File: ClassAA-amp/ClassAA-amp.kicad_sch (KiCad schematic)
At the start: 0 parts

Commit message: 回路図大体完成
定数は未決定
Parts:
- added C1, C2, C3, C4, C5, C6, C7, C8: C, symbol Device:C
- added J1, J2: AudioJack3, symbol Connector_Audio:AudioJack3
- added J3: Conn_01x03_Pin, symbol Connector:Conn_01x03_Pin
- added R1, R10, R11, R12, R13, R14, R15, R16, R2, R3, R4, R5, R6, R7, R8, R9: R, symbol Device:R
- added RV1: R_Potentiometer_Dual_Separate, symbol Device:R_Potentiometer_Dual_Separate
- added U1, U2: Opamp_Dual, symbol Device:Opamp_Dual
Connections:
- new net: R1.1, R2.1, U1.3 (+), U1.7
- new net: C1.2, R2.2, R4.1, R5.1, R6.2
- new net: R3.2, R4.2, U1.2 (-)
- new net: R1.2, R3.1, U1.1
- new net: R10.2, R12.1, U2.1
- new net: R12.2, R13.2, U2.2 (-)
- new net: C2.1, R8.1, R9.1, U2.6 (-)
- new net: C4.1, RV1.5
- new net: C4.2, R16.1, U2.5 (+)
- new net: C3.2, R15.1, U1.5 (+)
- new net: C1.1, R6.1, R7.1, U1.6 (-)
- new net: C3.1, RV1.2
- new net: C2.2, R11.2, R13.1, R14.1, R9.2
- new net: R10.1, R11.1, U2.3 (+), U2.7
- new net GND: C5.2, C6.1, C7.2, C8.1, J1.S, J2.S, J3.2 (Pin_2), R15.2, R16.2, R7.2, R8.2, RV1.3, RV1.6
- new net L_IN: J1.T, RV1.4
- new net L_OUT: J2.T, R14.2
- new net R_IN: J1.R, RV1.1
- new net R_OUT: J2.R, R5.2
- new net VDD: C5.1, C7.1, J3.1 (Pin_1), U1.8 (V+), U2.8 (V+)
- new net VEE: C6.2, C8.2, J3.3 (Pin_3), U1.4 (V-), U2.4 (V-)

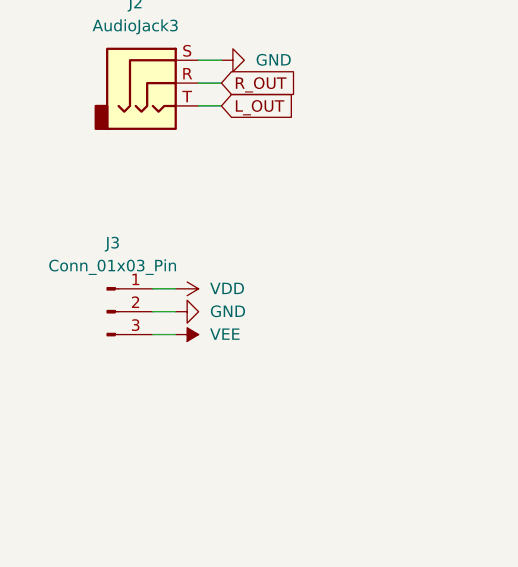
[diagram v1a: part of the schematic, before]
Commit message: コネクタのシンボル変更
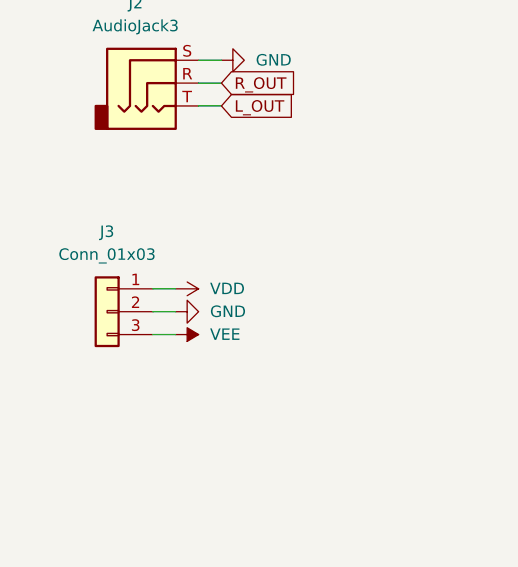
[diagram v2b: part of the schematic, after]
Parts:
- removed J3: Conn_01x03_Pin, symbol Connector:Conn_01x03_Pin
- added J3: Conn_01x03, symbol Connector_Generic:Conn_01x03
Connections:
- net GND: now also J3.2 (Pin_2)
- net VDD: now also J3.1 (Pin_1)
- net VEE: now also J3.3 (Pin_3)

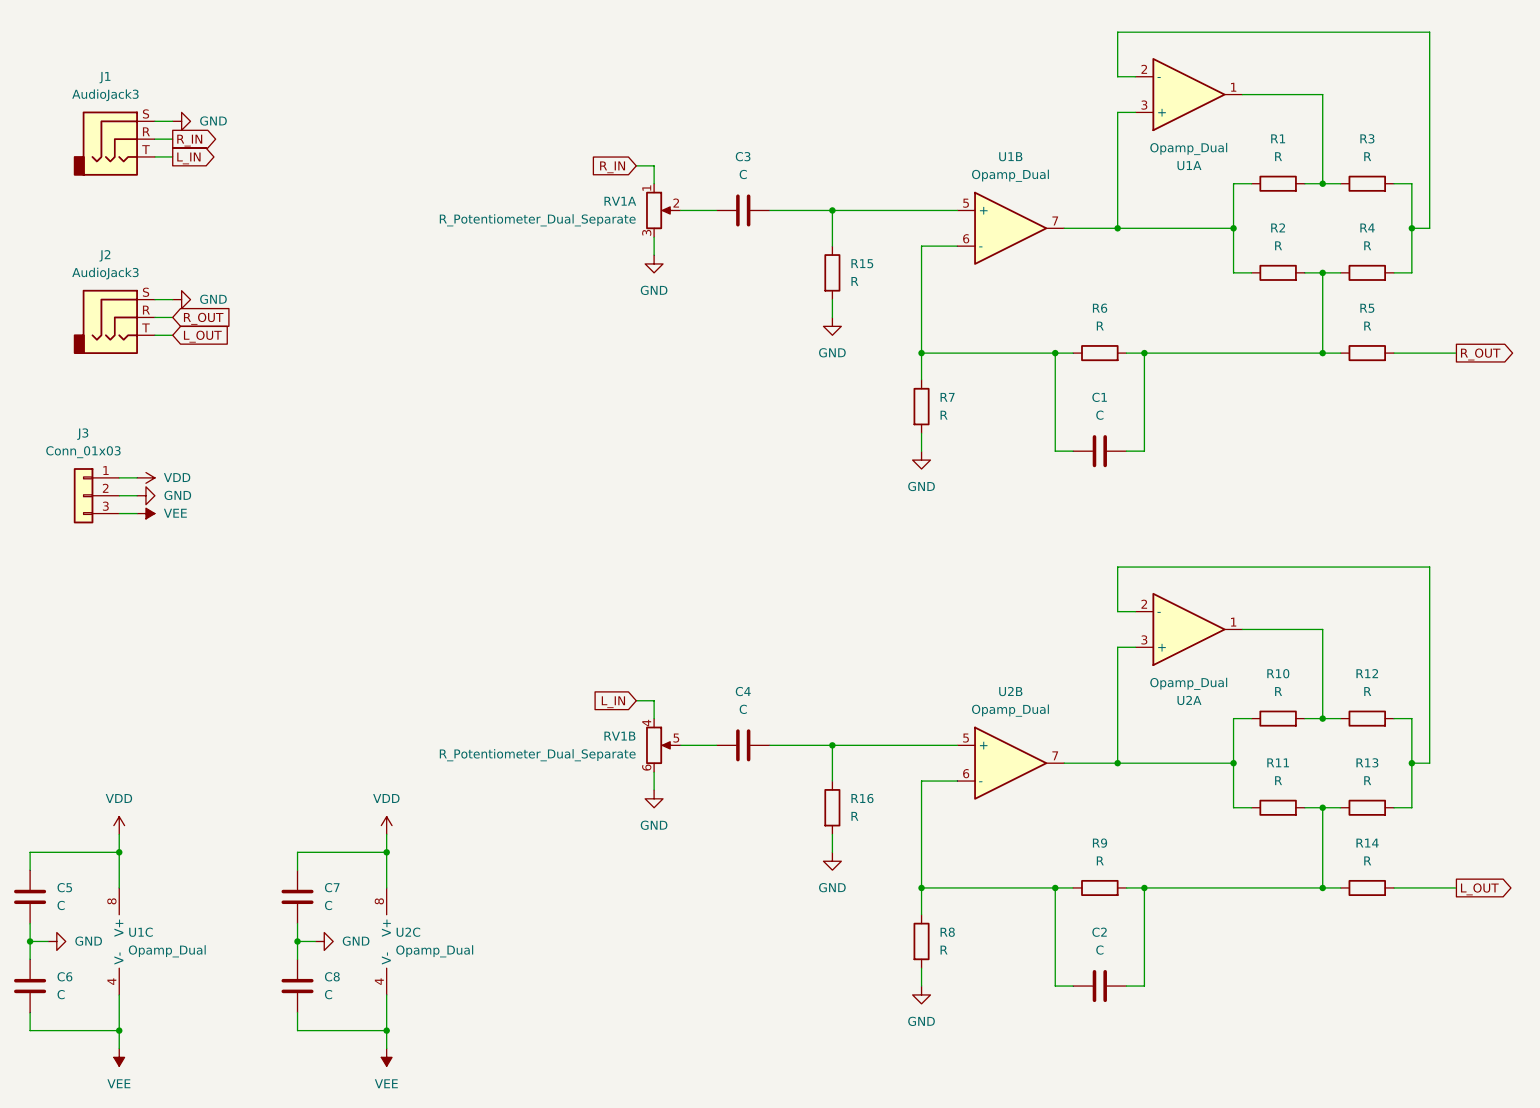
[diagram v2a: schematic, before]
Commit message: 定数決めとアノテーション
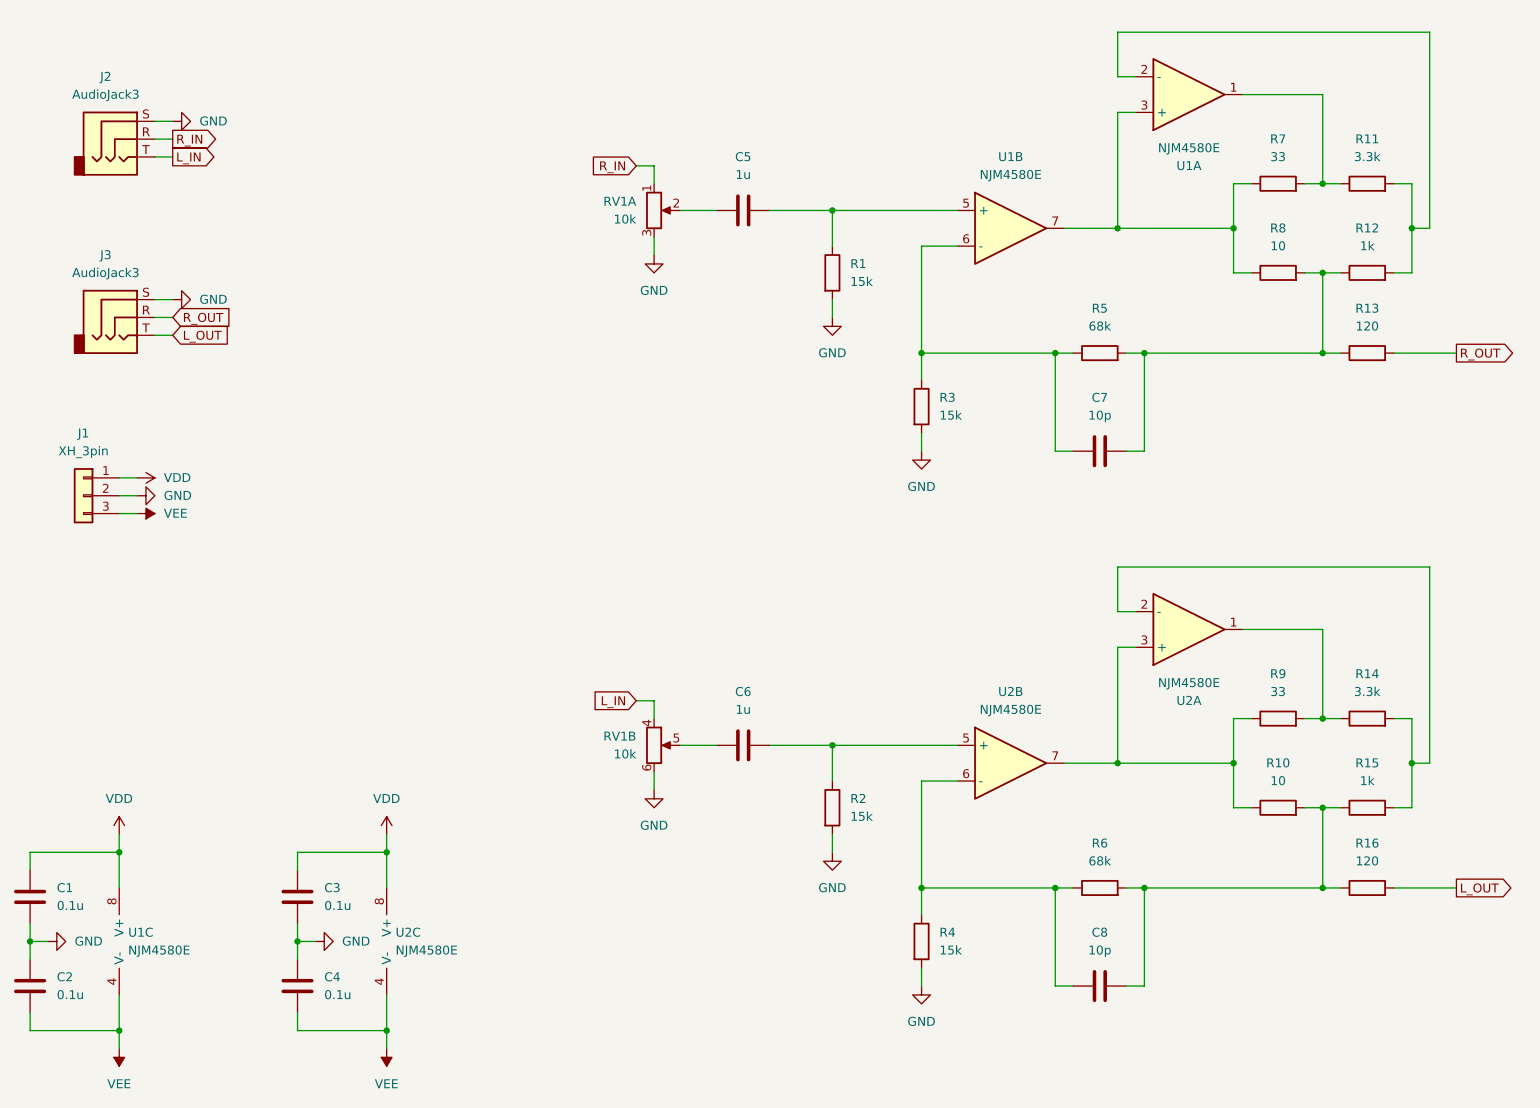
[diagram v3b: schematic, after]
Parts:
- C1: renamed from C5; value C -> 0.1u
- C2: renamed from C6; value C -> 0.1u
- C3: renamed from C7; value C -> 0.1u
- C4: renamed from C8; value C -> 0.1u
- C5: renamed from C3; value C -> 1u
- C6: renamed from C4; value C -> 1u
- C7: renamed from C1; value C -> 10p
- C8: renamed from C2; value C -> 10p
- J1: renamed from J3; value Conn_01x03 -> XH_3pin
- R1: renamed from R15; value R -> 15k
- R10: renamed from R11; value R -> 10
- R11: renamed from R3; value R -> 3.3k
- R12: renamed from R4; value R -> 1k
- R13: renamed from R5; value R -> 120
- R14: renamed from R12; value R -> 3.3k
- R15: renamed from R13; value R -> 1k
- R16: renamed from R14; value R -> 120
- R2: renamed from R16; value R -> 15k
- R3: renamed from R7; value R -> 15k
- R4: renamed from R8; value R -> 15k
- R5: renamed from R6; value R -> 68k
- R6: renamed from R9; value R -> 68k
- R7: renamed from R1; value R -> 33
- R8: renamed from R2; value R -> 10
- R9: renamed from R10; value R -> 33
- RV1: value R_Potentiometer_Dual_Separate -> 10k
- U1, U2: value Opamp_Dual -> NJM4580E
- renumbered J1 to J2, J2 to J3

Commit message: 位相補償の値変更、とりあえずは未実装
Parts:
- C7, C8: value 10p -> 6.8p; now not fitted
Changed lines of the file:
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@@
   )
   (symbol (lib_id "Device:C") (at 190.5 158.75 90) (unit 1)
-    (in_bom yes) (on_board yes) (dnp no) (fields_autoplaced)
+    (in_bom yes) (on_board yes) (dnp yes) (fields_autoplaced)
     (property "Reference" "C8" (at 190.5 151.13 90)
       (effects (font (size 1.27 1.27)))
     )
-    (property "Value" "10p" (at 190.5 153.67 90)
+    (property "Value" "6.8p" (at 190.5 153.67 90)
       (effects (font (size 1.27 1.27)))
     )
@@
   )
   (symbol (lib_id "Device:C") (at 190.5 82.55 90) (unit 1)
-    (in_bom yes) (on_board yes) (dnp no) (fields_autoplaced)
+    (in_bom yes) (on_board yes) (dnp yes) (fields_autoplaced)
     (property "Reference" "C7" (at 190.5 74.93 90)
       (effects (font (size 1.27 1.27)))
     )
-    (property "Value" "10p" (at 190.5 77.47 90)
-      (effects (font (size 1.27 1.27)))
-    )
+    (property "Value" "6.8p" (at 190.5 77.47 90)
+      (effects (font (size 1.27 1.27)))
+    )

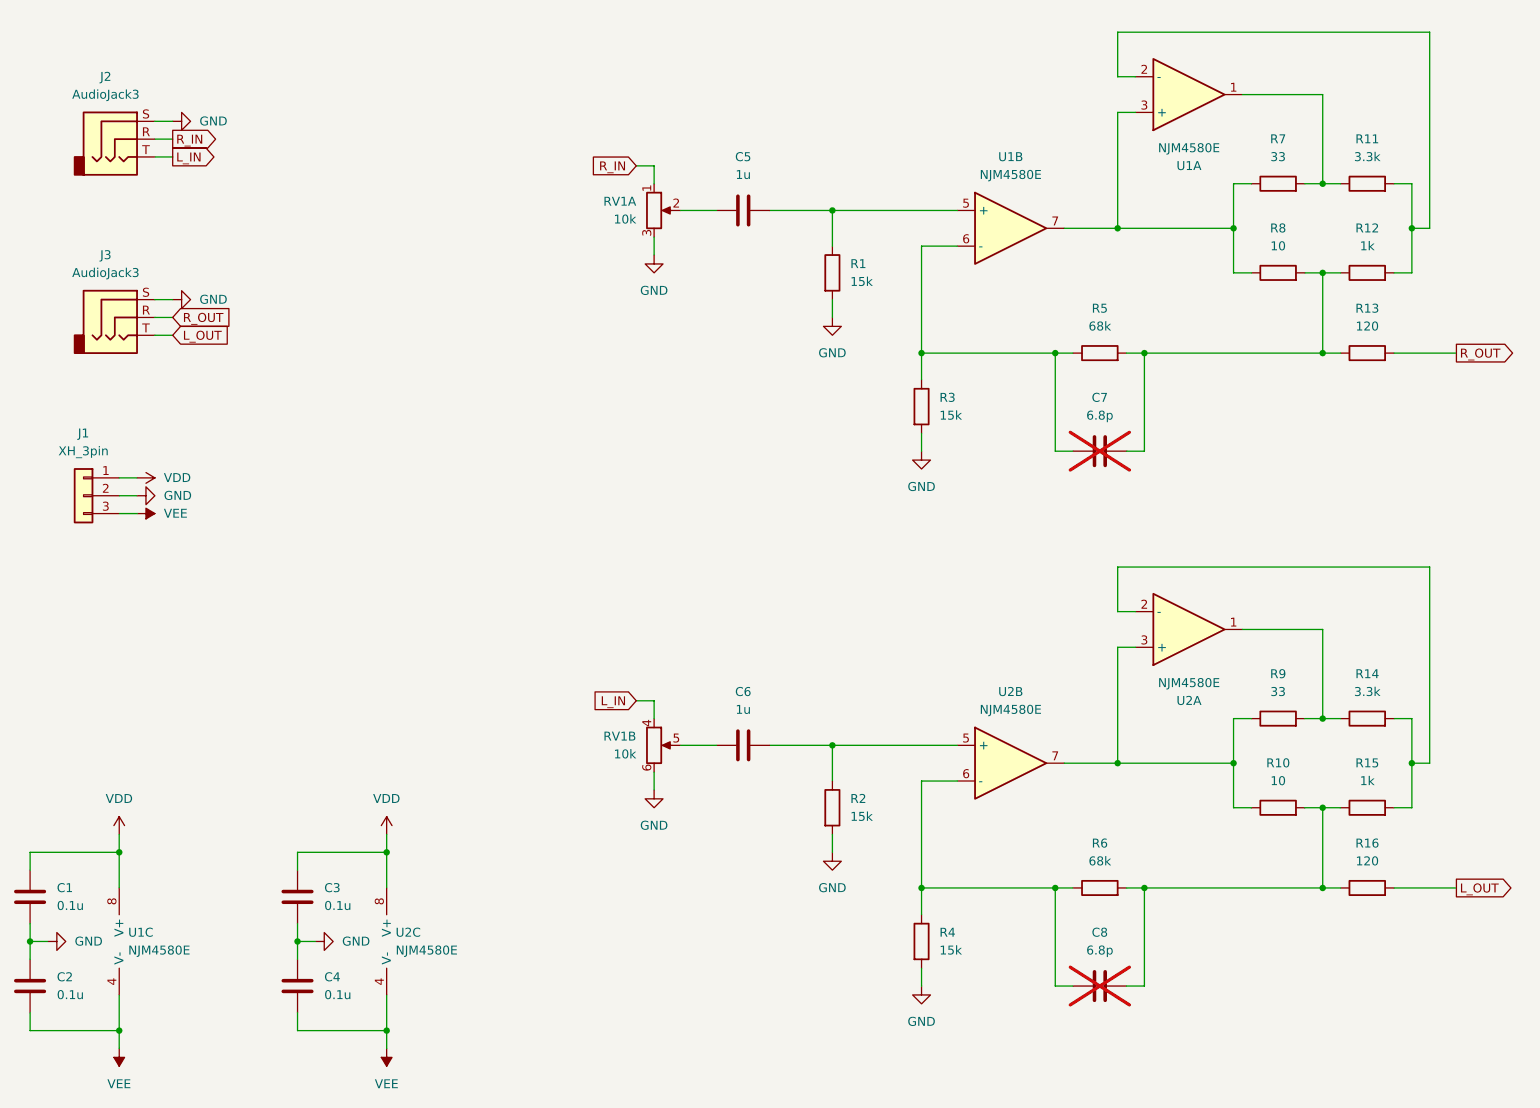
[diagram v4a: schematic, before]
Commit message: C-ampをNJM4580からNJM4556に変更
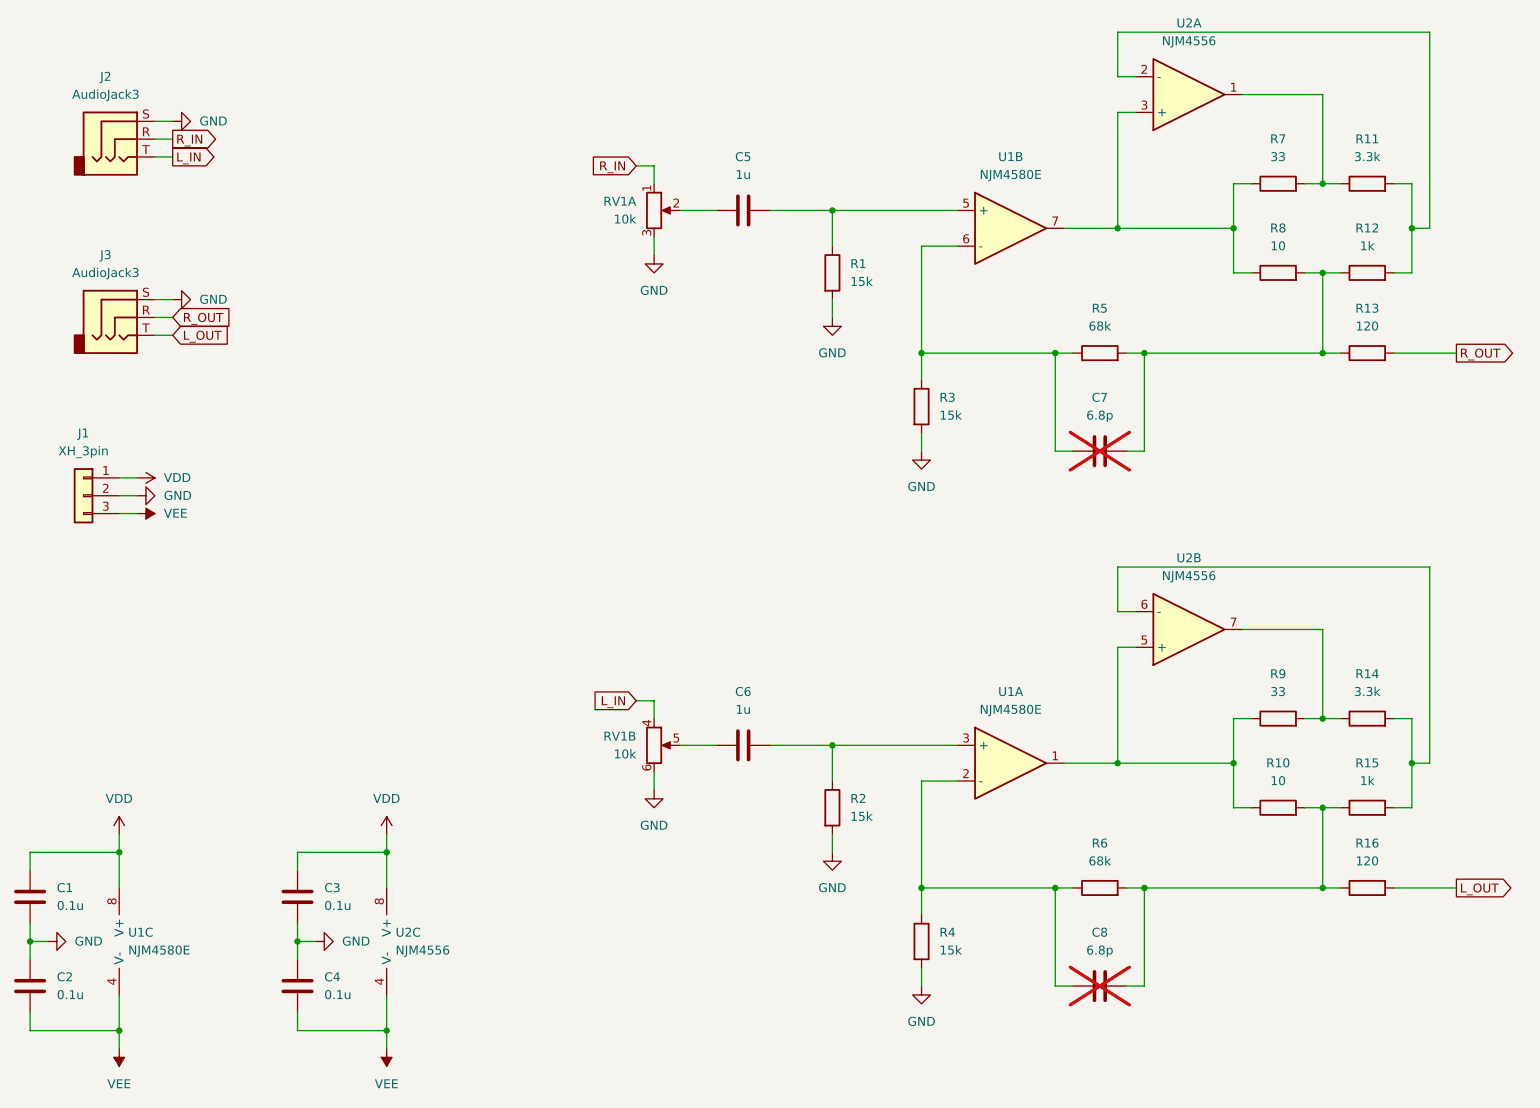
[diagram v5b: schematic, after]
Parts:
- U2: value NJM4580E -> NJM4556
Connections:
- net at R7.1, R8.1, U1.7: now also U2.3 (+); no longer U1.3 (+)
- net at R11.2, R12.2: now also U2.2 (-); no longer U1.2 (-)
- net at R11.1, R7.2: now also U2.1; no longer U1.1
- net at R14.1, R9.2: now also U2.7; no longer U2.1
- net at R14.2, R15.2: now also U2.6 (-); no longer U2.2 (-)
- net at C8.1, R4.1, R6.1: now also U1.2 (-); no longer U2.6 (-)
- net at C6.2, R2.1: now also U1.3 (+); no longer U2.5 (+)
- net at R10.1, R9.1: now also U1.1, U2.5 (+); no longer U2.3 (+), U2.7
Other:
- moved on the sheet: U1A
